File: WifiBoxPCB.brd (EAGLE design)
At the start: 65 x 30 mm, 4 parts, among them J1 CONNECTOR_PI_40_PIN, J3 OLED, J4 503182-1852, U1 OLED_I2C

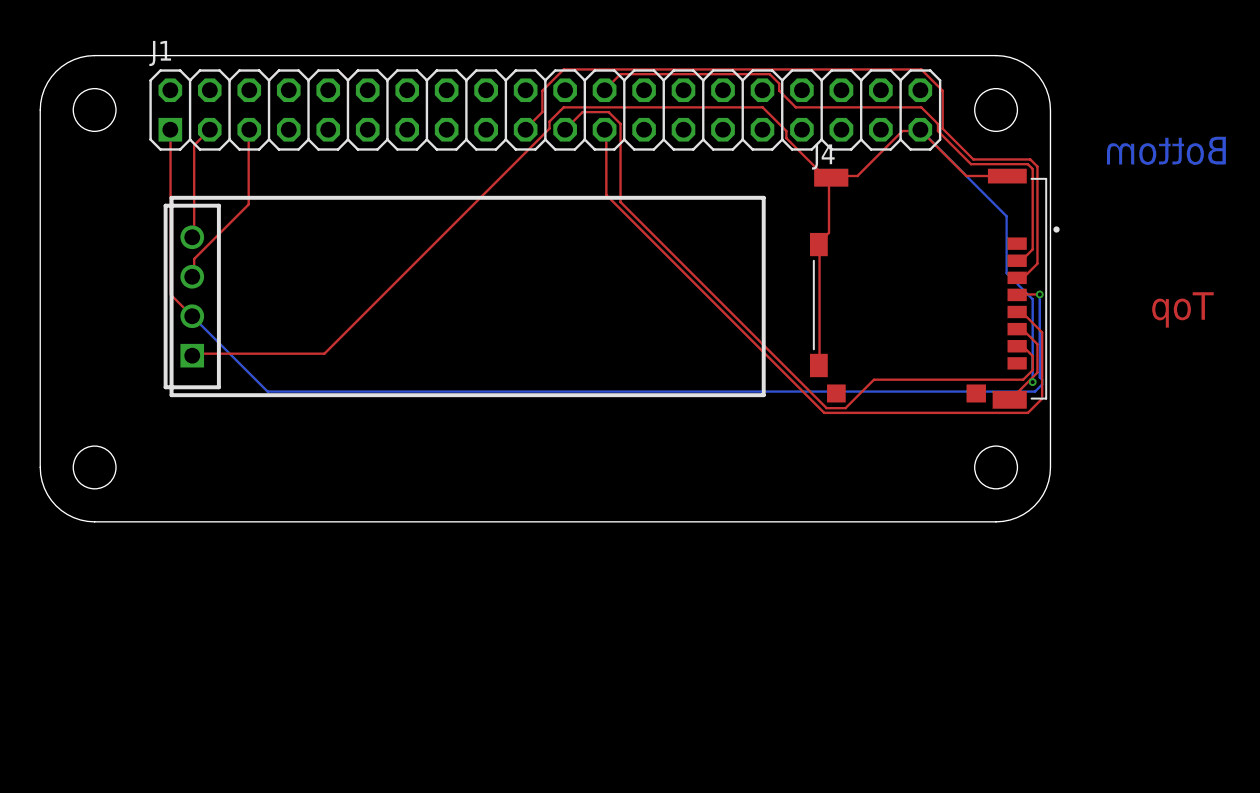
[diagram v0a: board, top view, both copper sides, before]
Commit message: 3rd round of updates removing the OLED
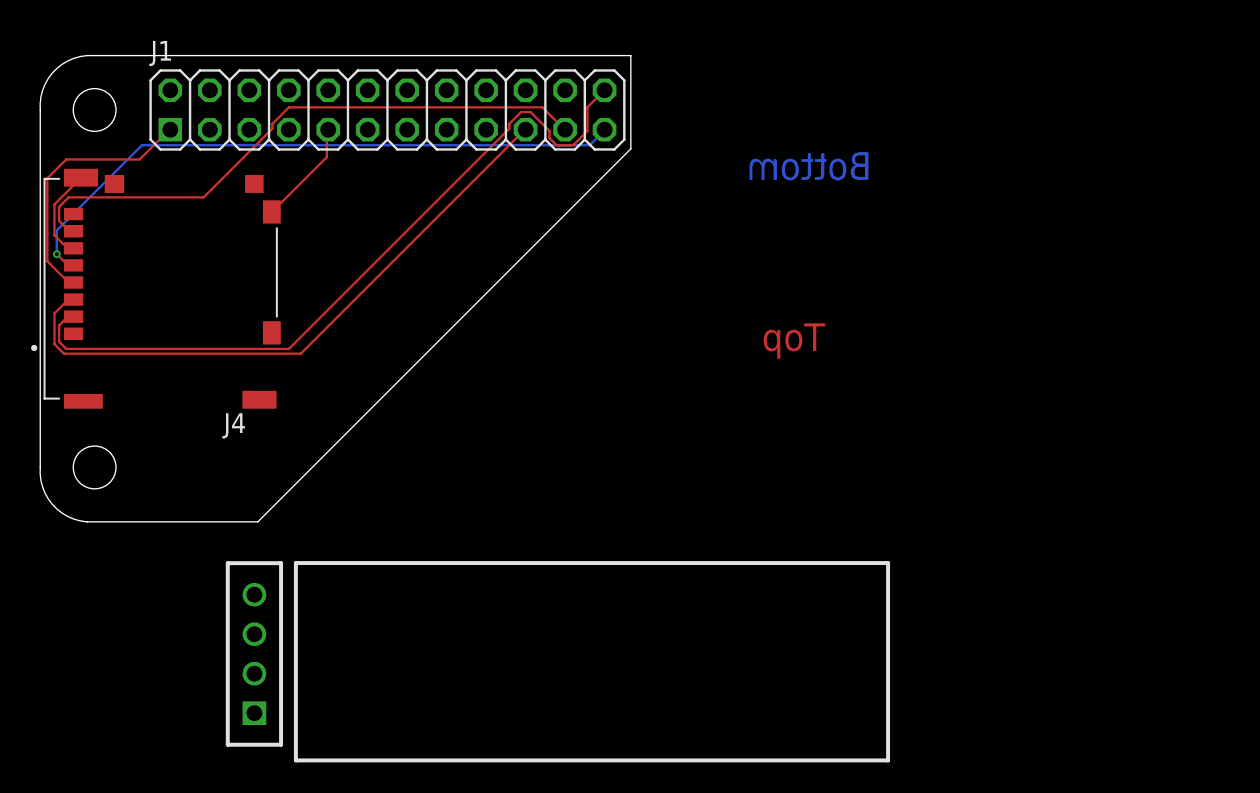
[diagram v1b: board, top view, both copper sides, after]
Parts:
- J1: value CONNECTOR_PI_40_PIN -> CONNECTOR_PI_24_PIN; device ConnectBox_2019:2X20 -> ConnectBox_2019:2X12
- moved J4 48.0 mm to (8.50, 15.0), turned to 90 degrees
- moved U1 24.8 mm to (35.5, -9.00)
- moved J3 23.3 mm to (13.8, -8.50)
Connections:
- removed net SCK: J1.5, J3.3
- removed net SDA: J1.3, J3.4
- net +3V3: no longer J3.2
- net GND: now also J1.9; no longer J1.39, J3.1
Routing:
- net GND: track 102.2 -> 12.8 mm, vias 1 -> 0
- net +3V3: track 76.8 -> 16.9 mm, vias 1 -> 0
- net SCK: track 11.0 -> 0.00 mm
- net CS: track 37.5 -> 47.5 mm
- net SDA: track 7.39 -> 0.00 mm
- net MOSI: track 47.3 -> 40.2 mm
- net MISO: track 44.6 -> 38.1 mm
- net SCLK: track 44.9 -> 40.9 mm, vias 0 -> 1
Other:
- board size 65 x 30 mm -> 38 x 30 mm
